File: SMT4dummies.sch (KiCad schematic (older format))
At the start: 54 parts, among them IC1 4520, IC2 LM2902N, IC3 LM555N, J1 USB_2, P1 CONN_2, Q1 NPN, Q2 NPN, Q3 NPN, Q4 NPN, SW1 SW_PUSH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

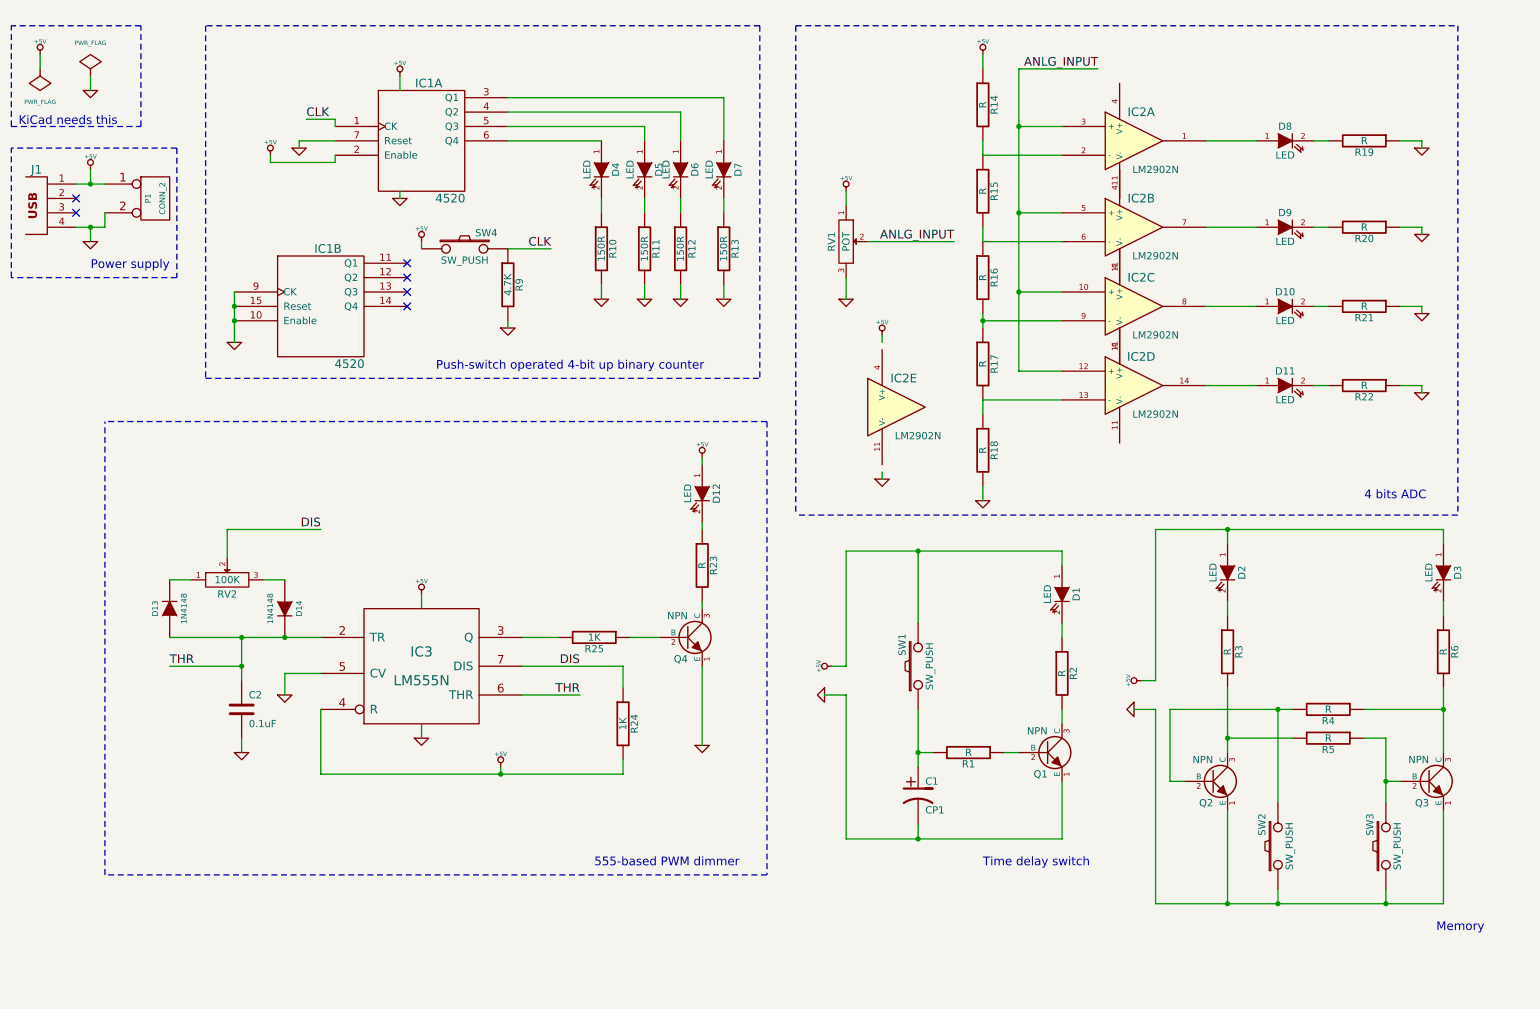
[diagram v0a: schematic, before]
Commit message: SMT4dummies logo added, some improvements on the silkscreen
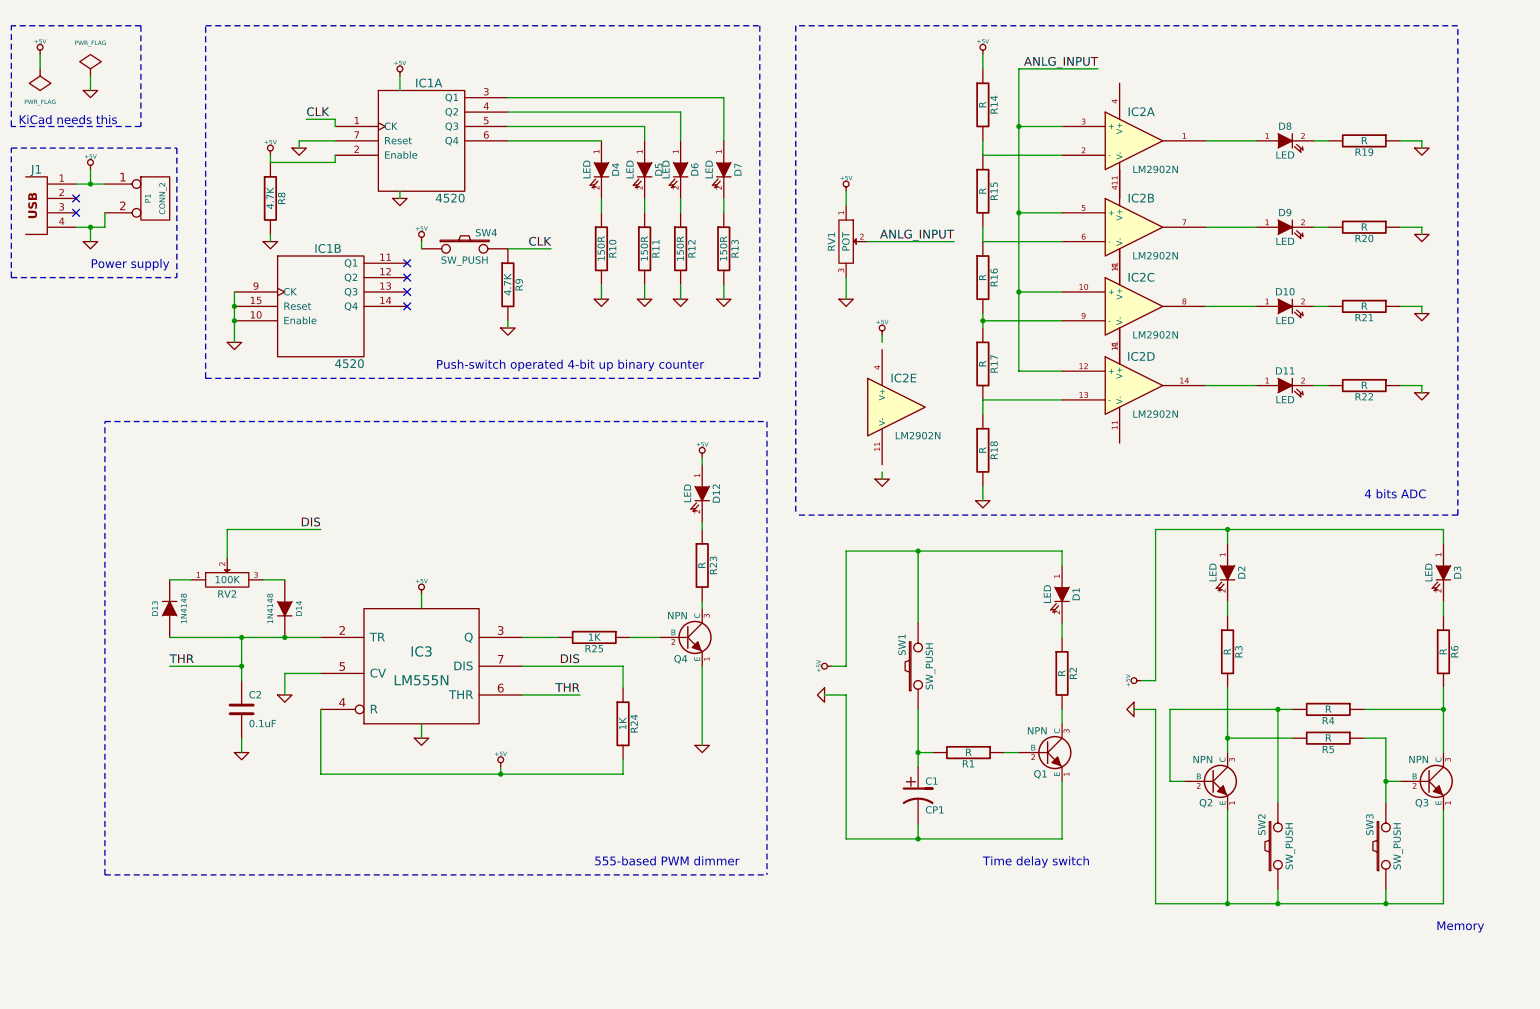
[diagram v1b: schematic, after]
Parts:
- added R8: 4.7K, symbol R
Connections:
- net +5V: now also R8.1
- net GND: now also R8.2

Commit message: Fixed pull-up resistor postion on schematic.
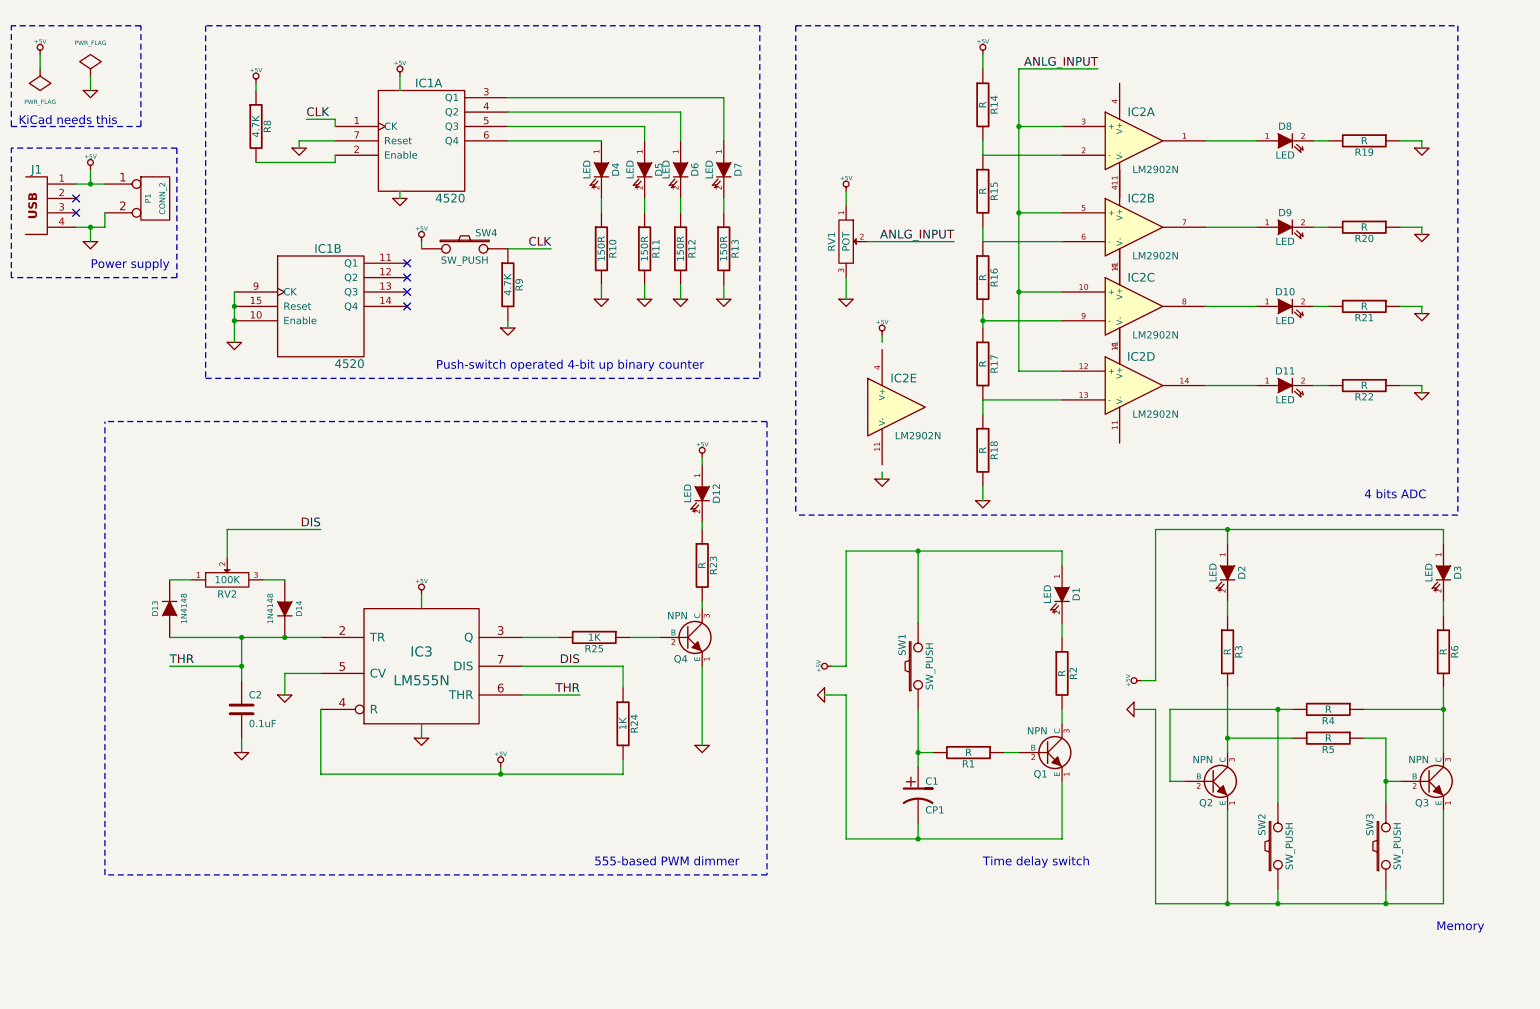
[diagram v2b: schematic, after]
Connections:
- net +5V: no longer IC1.2 (Enable)
- net GND: no longer R8.2
- new net: IC1.2 (Enable), R8.2
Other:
- moved on the sheet: R8

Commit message: Schematic fixed. Values added. Netlist updated.
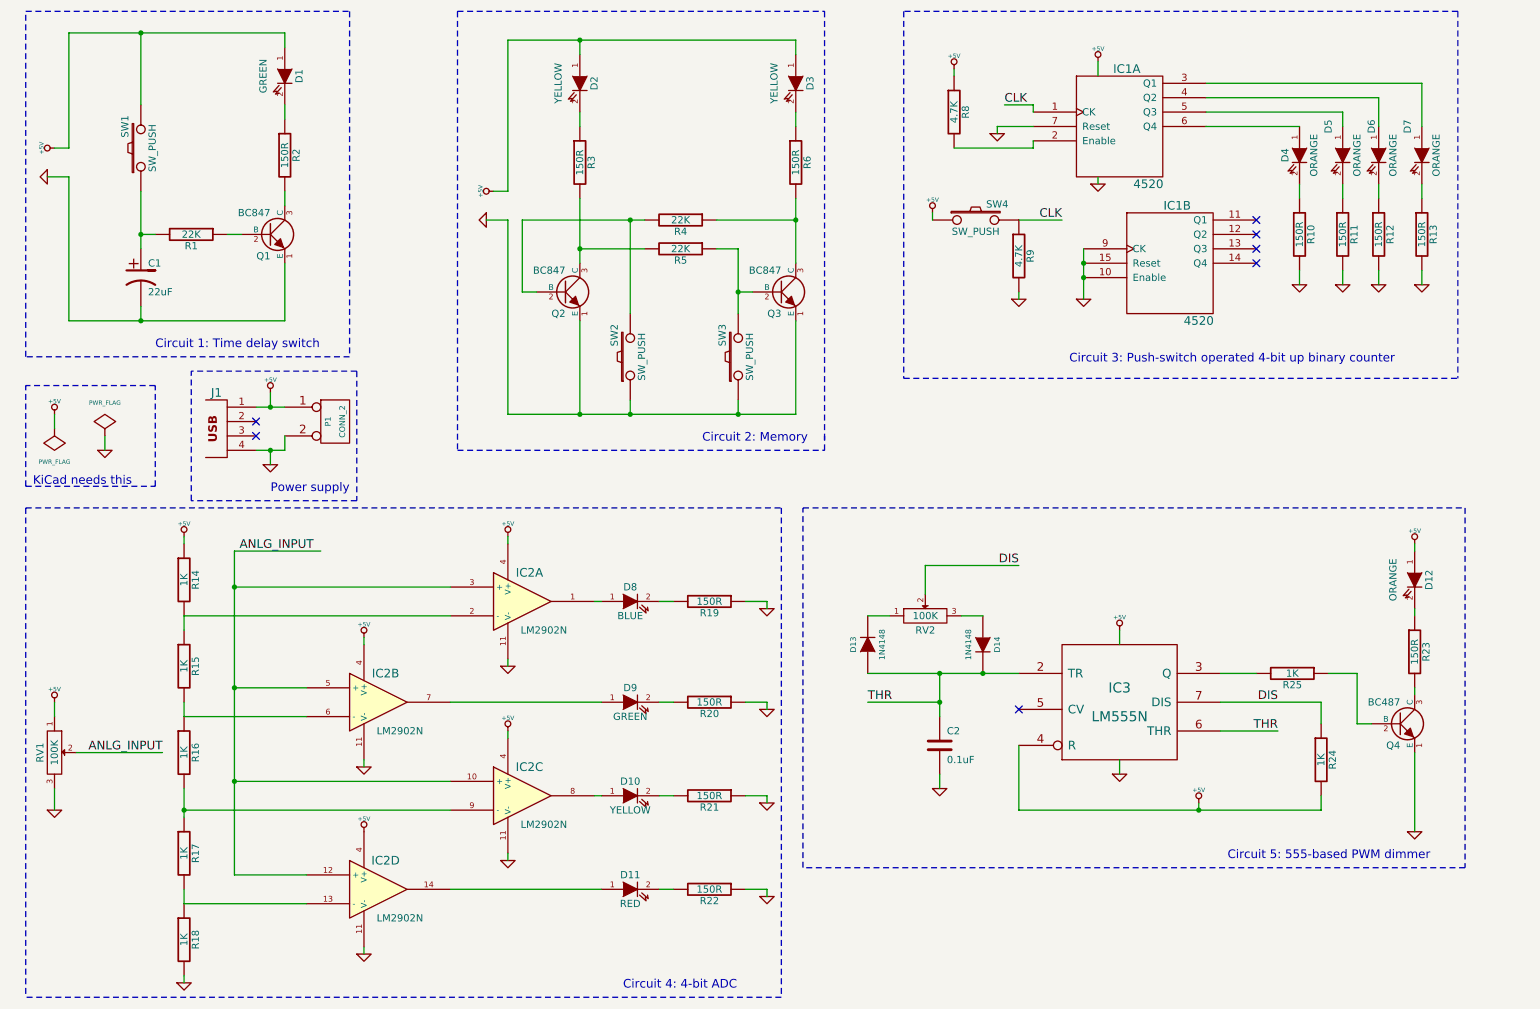
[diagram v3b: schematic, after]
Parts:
- removed unit 5 of IC2
- C1: value CP1 -> 22uF
- D1, D9: value LED -> GREEN
- D10, D2, D3: value LED -> YELLOW
- D11: value LED -> RED
- D12, D4, D5, D6, D7: value LED -> ORANGE
- D8: value LED -> BLUE
- Q1, Q2, Q3: value NPN -> BC847
- Q4: value NPN -> BC487
- R1, R4, R5: value R -> 22K
- R14, R15, R16, R17, R18: value R -> 1K
- R19, R2, R20, R21, R22, R23, R3, R6: value R -> 150R
- RV1: value POT -> 100K
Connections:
- net +5V: now also IC2.4 (V+), IC2.4 (V+), IC2.4 (V+), IC2.4 (V+)
- net GND: now also IC2.11 (V-), IC2.11 (V-), IC2.11 (V-), IC2.11 (V-); no longer IC3.5 (CV)
- no-connect marks 6 -> 7
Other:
- note added: "Circuit 1: Time delay switch"
- note added: "Circuit 2: Memory\n"
- note added: "Circuit 3: Push-switch operated 4-bit up binary counter"
- note added: "Circuit 4: 4-bit ADC"
- note added: "Circuit 5: 555-based PWM dimmer"
- note removed: "4 bits ADC"
- note removed: "555-based PWM dimmer"
- note removed: "Memory\n"
- note removed: "Push-switch operated 4-bit up binary counter"
- note removed: "Time delay switch"
- moved on the sheet: C1, C2, D1, D10, D11, D12, D13, D14, D2, D3, D4, D5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

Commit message: Transistor polarity error fixed
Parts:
- removed Q1, Q2, Q3: BC847, symbol NPN
- removed Q4: BC487, symbol NPN
- added Q1, Q2, Q3, Q4: BC847, SOT-23, symbol BC849
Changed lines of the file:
@@
-EESchema Schematic File Version 2  date Sat 08 Jun 2013 01:57:34 CEST
+EESchema Schematic File Version 2  date Mon 01 Jul 2013 06:51:39 PM CEST
 LIBS:power
 LIBS:device
@@
 LIBS:npn
 LIBS:SMT4dummies-cache
-EELAYER 24 0
+EELAYER 27 0
 EELAYER END
 $Descr A4 11693 8268
@@
 Sheet 1 1
 Title "SMT4dummies"
-Date "7 jun 2013"
+Date "1 jul 2013"
 Rev "2"
 Comp "d-Squared Robotics"
@@
 NoConn ~ 9450 2300
 NoConn ~ 9450 2400
-$Comp
-L NPN Q2
-U 1 1 512D297D
-P 4650 2600
-F 0 "Q2" H 4650 2450 50  0000 R CNN
-F 1 "BC847" H 4650 2750 50  0000 R CNN
-F 2 "" H 4650 2600 60  0001 C CNN
-F 3 "" H 4650 2600 60  0001 C CNN
-	1    4650 2600
-	1    0    0    -1
-$EndComp
-$Comp
-L NPN Q3
-U 1 1 512D297A
-P 6150 2600
-F 0 "Q3" H 6150 2450 50  0000 R CNN
-F 1 "BC847" H 6150 2750 50  0000 R CNN
-F 2 "" H 6150 2600 60  0001 C CNN
-F 3 "" H 6150 2600 60  0001 C CNN
-	1    6150 2600
-	1    0    0    -1
-$EndComp
-$Comp
-L NPN Q1
-U 1 1 512D2975
-P 2600 2200
-F 0 "Q1" H 2600 2050 50  0000 R CNN
-F 1 "BC847" H 2600 2350 50  0000 R CNN
-F 2 "" H 2600 2200 60  0001 C CNN
-F 3 "" H 2600 2200 60  0001 C CNN
-	1    2600 2200
-	1    0    0    -1
-$EndComp
-$Comp
-L NPN Q4
-U 1 1 512D2965
-P 10450 5600
-F 0 "Q4" H 10450 5450 50  0000 R CNN
-F 1 "BC487" H 10450 5750 50  0000 R CNN
-F 2 "" H 10450 5600 60  0001 C CNN
-F 3 "" H 10450 5600 60  0001 C CNN
-	1    10450 5600
-	1    0    0    -1
-$EndComp
 $Comp
 L R R2
@@
 	4250 5700 4250 5650
 Wire Wire Line
-	2000 6250 2000 6050
+	2000 6050 2000 6250
 $Comp
 L +5V #PWR042
@@
 Wire Wire Line
 	2850 5550 2000 5550
+$Comp
+L BC849 Q3
+U 1 1 51D1B1A1
+P 6150 2600
+F 0 "Q3" H 6150 2749 40  0000 R CNN
+F 1 "BC847" H 6150 2450 40  0000 R CNN
+F 2 "SOT-23" H 6050 2498 29  0000 C CNN
+F 3 "~" H 6150 2600 60  0000 C CNN
+	1    6150 2600
+	1    0    0    -1
+$EndComp
+$Comp
+L BC849 Q2
+U 1 1 51D1B1D6
+P 4650 2600
+F 0 "Q2" H 4650 2749 40  0000 R CNN
+F 1 "BC847" H 4650 2450 40  0000 R CNN
+F 2 "SOT-23" H 4550 2498 29  0000 C CNN
+F 3 "~" H 4650 2600 60  0000 C CNN
+	1    4650 2600
+	1    0    0    -1
+$EndComp
+$Comp
+L BC849 Q1
+U 1 1 51D1B1E1
+P 2600 2200
+F 0 "Q1" H 2600 2349 40  0000 R CNN
+F 1 "BC847" H 2600 2050 40  0000 R CNN
+F 2 "SOT-23" H 2500 2098 29  0000 C CNN
+F 3 "~" H 2600 2200 60  0000 C CNN
+	1    2600 2200
+	1    0    0    -1
+$EndComp
+$Comp
+L BC849 Q4
+U 1 1 51D1B1EC
+P 10450 5600
+F 0 "Q4" H 10450 5749 40  0000 R CNN
+F 1 "BC847" H 10450 5450 40  0000 R CNN
+F 2 "SOT-23" H 10350 5498 29  0000 C CNN
+F 3 "~" H 10450 5600 60  0000 C CNN
+	1    10450 5600
+	1    0    0    -1
+$EndComp
 $EndSCHEMATC
